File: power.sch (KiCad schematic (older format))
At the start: 14 parts, among them U3 XC6206, U4 MAX40200AUK, U5 MAX40200AUK, U6 TPS63001

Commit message: Add digikey pn's to schematic, update BOM
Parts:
- C10, C11: Digikey (none) -> 490-14381-1-ND
- C5, C6: Digikey (none) -> 311-1439-1-ND
- C7, C8: Digikey (none) -> 490-14466-1-ND
- C9: Digikey (none) -> 490-14603-1-ND
- L1: Digikey (none) -> 490-2501-1-ND
- R11: Digikey (none) -> 311-100LRTR-ND
- R12: Digikey (none) -> 311-0.0JRCT-ND
- U3: Digikey (none) -> MCP1700T3302ETTCT-ND
- U4, U5: Digikey (none) -> MAX40200AUK+TCT-ND
- U6: Digikey (none) -> 296-19643-1-ND
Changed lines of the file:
@@
 F 3 "http://ww1.microchip.com/downloads/en/DeviceDoc/20005122B.pdf" H 2100 3500 50  0001 C CNN
 F 4 "C5446" H 2100 3550 50  0001 C CNN "LCSC"
+F 5 "MCP1700T3302ETTCT-ND" H 2100 3550 50  0001 C CNN "Digikey"
 	1    2100 3550
 	1    0    0    -1
@@
 F 3 "~" H 1450 3900 50  0001 C CNN
 F 4 "C52923" H 1450 3900 50  0001 C CNN "LCSC"
+F 5 "311-1439-1-ND" H 1450 3900 50  0001 C CNN "Digikey"
 	1    1450 3900
 	1    0    0    -1
@@
 F 3 "http://www.ti.com/lit/ds/symlink/tps63000.pdf" H 7400 4150 50  0001 C CNN
 F 4 "C28060" H 7700 3600 50  0001 C CNN "LCSC"
+F 5 "296-19643-1-ND" H 7700 3600 50  0001 C CNN "Digikey"
 	1    7700 3600
 	1    0    0    -1
@@
 F 3 "~" H 7700 2600 50  0001 C CNN
 F 4 "C86074" V 7700 2600 50  0001 C CNN "LCSC"
+F 5 "490-2501-1-ND" V 7700 2600 50  0001 C CNN "Digikey"
 	1    7700 2600
 	0    -1   -1   0
@@
 F 3 "~" H 6650 3650 50  0001 C CNN
 F 4 "C25076" H 6650 3650 50  0001 C CNN "LCSC"
+F 5 "311-100LRTR-ND" H 6650 3650 50  0001 C CNN "Digikey"
 	1    6650 3650
 	1    0    0    -1
@@
 F 3 "~" H 6650 4150 50  0001 C CNN
 F 4 "C1525" H 6650 4150 50  0001 C CNN "LCSC"
+F 5 "490-14603-1-ND" H 6650 4150 50  0001 C CNN "Digikey"
 	1    6650 4150
 	1    0    0    -1
@@
 F 3 "~" H 5750 3750 50  0001 C CNN
 F 4 "C1779" H 5750 3750 50  0001 C CNN "LCSC"
+F 5 "490-14466-1-ND" H 5750 3750 50  0001 C CNN "Digikey"
 	1    5750 3750
 	1    0    0    -1
@@
 F 3 "~" H 9250 3700 50  0001 C CNN
 F 4 "C15850" H 9250 3700 50  0001 C CNN "LCSC"
+F 5 "490-14381-1-ND" H 9250 3700 50  0001 C CNN "Digikey"
 	1    9250 3700
 	1    0    0    -1
@@
 F 3 "https://datasheets.maximintegrated.com/en/ds/MAX40200.pdf" H 4750 4000 50  0001 C CNN
 F 4 "" H 4750 3500 50  0001 C CNN "LCSC"
+F 5 "MAX40200AUK+TCT-ND" H 4750 3500 50  0001 C CNN "Digikey"
 	1    4750 3500
 	1    0    0    -1
@@
 F 3 "https://datasheets.maximintegrated.com/en/ds/MAX40200.pdf" H 4750 2650 50  0001 C CNN
 F 4 "" H 4750 2150 50  0001 C CNN "LCSC"
+F 5 "MAX40200AUK+TCT-ND" H 4750 2150 50  0001 C CNN "Digikey"
 	1    4750 2150
 	1    0    0    -1
@@
 F 3 "~" H 8650 5150 50  0001 C CNN
 F 4 "C17168" V 8650 5150 50  0001 C CNN "LCSC"
+F 5 "311-0.0JRCT-ND" V 8650 5150 50  0001 C CNN "Digikey"
 	1    8650 5150
 	0    1    1    0
@@
 F 3 "~" H 2750 3900 50  0001 C CNN
 F 4 "C52923" H 2750 3900 50  0001 C CNN "LCSC"
+F 5 "311-1439-1-ND" H 2750 3900 50  0001 C CNN "Digikey"
 	1    2750 3900
 	1    0    0    -1
@@
 F 3 "~" H 6200 3750 50  0001 C CNN
 F 4 "C1779" H 6200 3750 50  0001 C CNN "LCSC"
+F 5 "490-14466-1-ND" H 6200 3750 50  0001 C CNN "Digikey"
 	1    6200 3750
 	1    0    0    -1
@@
 F 3 "~" H 9650 3700 50  0001 C CNN
 F 4 "C15850" H 9650 3700 50  0001 C CNN "LCSC"
+F 5 "490-14381-1-ND" H 9650 3700 50  0001 C CNN "Digikey"
 	1    9650 3700
 	1    0    0    -1
@@
 USB 3V3
 $Comp
-L Graphic:Logo_Open_Hardware_Small #LOGO?
+L Graphic:Logo_Open_Hardware_Small #LOGO3
 U 1 1 5DD3609E
 P 10900 6900
-F 0 "#LOGO?" H 10900 7175 50  0001 C CNN
+F 0 "#LOGO3" H 10900 7175 50  0001 C CNN
 F 1 "Logo_Open_Hardware_Small" H 10900 6675 50  0001 C CNN
 F 2 "" H 10900 6900 50  0001 C CNN
@@
 $EndComp
 $Comp
-L Graphic:SYM_Radio_Waves_Large #SYM?
+L Graphic:SYM_Radio_Waves_Large #SYM3
 U 1 1 5DD360A4
 P 10350 6850
-F 0 "#SYM?" H 10350 7050 50  0001 C CNN
+F 0 "#SYM3" H 10350 7050 50  0001 C CNN
 F 1 "SYM_Radio_Waves_Large" H 10350 6600 50  0001 C CNN
 F 2 "" H 10350 6650 50  0001 C CNN

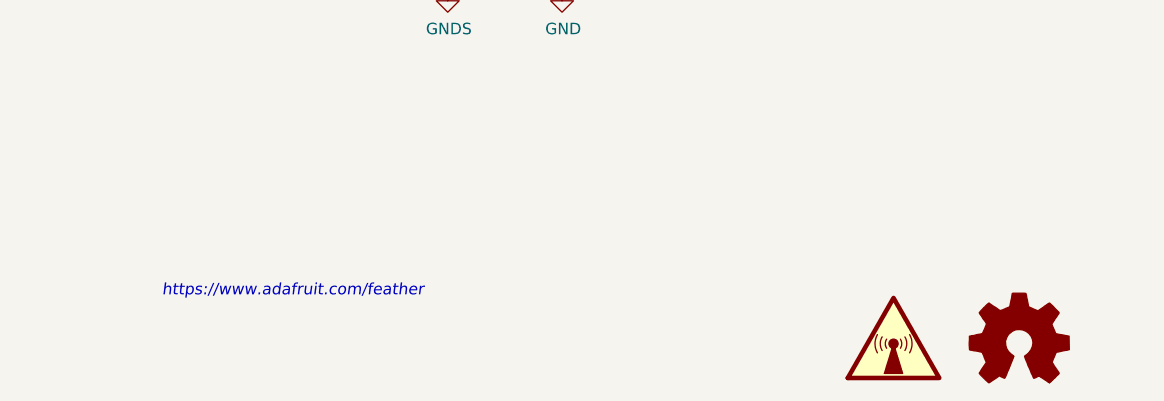
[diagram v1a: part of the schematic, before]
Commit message: PCB REV C0 * Make U8 footprint capable of crypto and fram device * Minor updates to schematic * Minor updates to doc prints * Update bot silk to REV C0
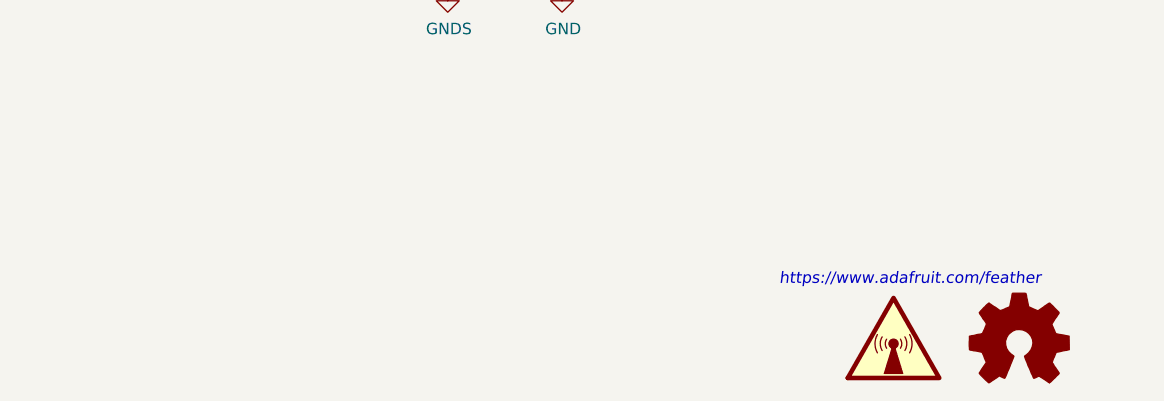
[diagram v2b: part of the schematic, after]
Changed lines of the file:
@@
 EndData
 $EndBitmap
-Text Notes 7150 6700 0    50   Italic 0
+Text Notes 9850 6650 0    50   Italic 0
 https://www.adafruit.com/feather
 $Bitmap
